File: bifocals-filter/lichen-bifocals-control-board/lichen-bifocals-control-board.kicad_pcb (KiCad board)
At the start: 2 copper layers, 37.8 x 108 mm, 18 parts, among them J1 EURO_JACK, J2 EURO_JACK, J3 EURO_JACK, J4 EURO_JACK, J5 EURO_JACK, J6 EURO_JACK, J7 EURO_JACK, J8 EURO_JACK, J9 EURO_JACK

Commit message: v1.1 of Freddie and Bifocals hardware.
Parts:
- added MH2: MountingHole_2.2mm_M2, MountingHole:MountingHole_2.2mm_M2, F.Cu at (113.2, 203.1)
- added MH2: MountingHole_2.2mm_M2, MountingHole:MountingHole_2.2mm_M2, F.Cu at (127.1, 203.1)
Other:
- board text added: "August 2024"
- board text added: "Lichen Community Systems Bifocals v1.1"
- board text removed: "February 2024"
- board text removed: "Lichen Community Systems Bifocals v1.0"

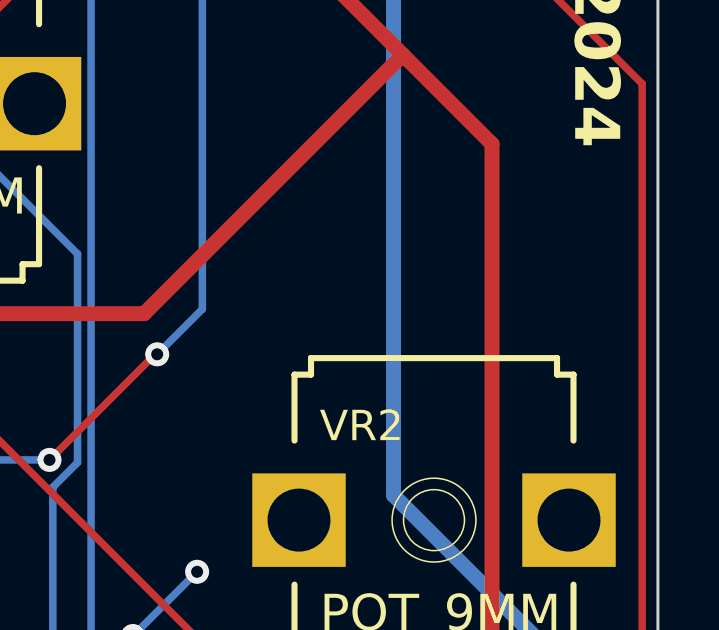
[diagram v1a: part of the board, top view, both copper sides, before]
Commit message: Updates Lichen component library and most module prototypes.
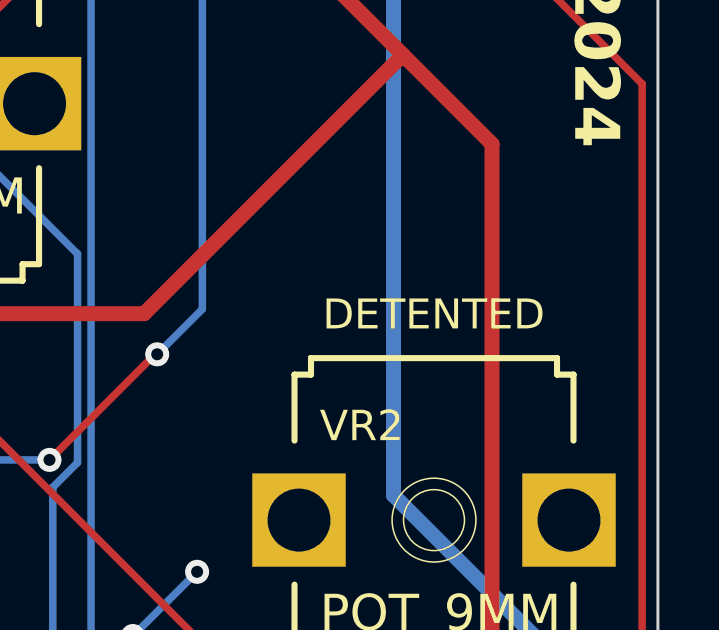
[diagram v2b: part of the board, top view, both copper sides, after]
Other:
- board text added: "DETENTED"
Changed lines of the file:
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@@
       (disableapertmacros false)
       (usegerberextensions true)
-      (usegerberattributes true)
-      (usegerberadvancedattributes true)
-      (creategerberjobfile true)
+      (usegerberattributes false)
+      (usegerberadvancedattributes false)
+      (creategerberjobfile false)
       (dashed_line_dash_ratio 12.000000)
       (dashed_line_gap_ratio 3.000000)
@@
       (psa4output false)
       (plotreference true)
-      (plotvalue true)
+      (plotvalue false)
       (plotinvisibletext false)
       (sketchpadsonfab false)
@@
       (drillshape 0)
       (scaleselection 1)
-      (outputdirectory "gerbers-lichen-bifocals-control-board-v1.0/")
+      (outputdirectory "Production/v1.1/")
     )
   )
@@
     )
   )
+  (gr_text "DETENTED" (at 127.87 131.79) (layer "F.SilkS")
+    (effects (font (size 1 1) (thickness 0.15)) (justify left bottom))
+  )
   (gr_text "Lichen Community Systems Bifocals v1.1\n" (at 101.67 110.78 270) (layer "F.SilkS")
